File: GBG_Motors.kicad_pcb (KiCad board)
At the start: 2 copper layers, 54 parts, among them J101 Input, J102 Seeed XIAO L, J103 Seeed XIAO R, J104 Pin, J105 Pout, J601 Limit Switch, J701 Limit Switch, Q602 NPN, Q701 NPN, U101 JK Controller, U102 HL Controller, U103 R-78E5.0-0.5, U601 NE555P, U701 NE555P

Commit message: Finished initial board design
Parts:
- JP103: footprint Jumper:SolderJumper-2_P1.3mm_Bridged_RoundedPad1.0x1.5mm -> Jumper:SolderJumper-2_P1.3mm_Open_RoundedPad1.0x1.5mm
- U102: moved to B.Cu
- moved J601 142.7 mm to (122.0, 73.2)
- moved JP603 131.8 mm to (139.5, 94.2)
- moved R607 128.8 mm to (131.9, 110.0), turned to 90 degrees
- moved U101 127.3 mm to (169.9, 101.2), turned to 90 degrees
- moved JP602 118.9 mm to (159.5, 103.9)
- moved U102 117.2 mm to (169.9, 80.4), turned to -90 degrees
- moved C602 115.3 mm to (131.9, 99.8), turned to 90 degrees
- moved U601 114.9 mm to (143.3, 107.4), turned to 180 degrees
- moved JP601 112.5 mm to (158.9, 108.7)
- moved R602 110.2 mm to (154.2, 102.4), turned to -90 degrees
- moved R605 109.7 mm to (147.1, 99.8), turned to 90 degrees
- moved R604 106.5 mm to (150.7, 92.2), turned to -90 degrees
- moved R601 101.1 mm to (161.3, 92.2), turned to -90 degrees
- moved R603 101.1 mm to (157.8, 92.2), turned to -90 degrees
- moved Q601 100.0 mm to (147.6, 104.9), turned to -90 degrees
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- renumbered JP602 to JP601, JP601 to JP602, JP802 to JP801, JP803 to JP802, Q602 to Q601, R607 to R605, R605 to R607
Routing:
- net +5V: track 0.00 -> 173.6 mm, vias 0 -> 6
- net GND: track 0.00 -> 112.2 mm, vias 0 -> 5
- net Hs: track 0.00 -> 71.9 mm
- net /HLBlockerH/input_limited: track 0.00 -> 63.9 mm
- net LRi: track 0.00 -> 60.1 mm, vias 0 -> 3
- net Vout: track 0.00 -> 56.6 mm
- net Kc: track 0.00 -> 56.1 mm, vias 0 -> 1
- net HRo: track 0.00 -> 51.4 mm, vias 0 -> 1
- net VDD: track 0.00 -> 49.7 mm, vias 0 -> 1
- net HRi: track 0.00 -> 48.7 mm, vias 0 -> 1
- net Ls: track 0.00 -> 46.2 mm
- net Jc: track 0.00 -> 46.1 mm, vias 0 -> 1
- net KRi: track 0.00 -> 43.2 mm, vias 0 -> 1
- net Hc: track 0.00 -> 38.2 mm, vias 0 -> 1
- net LRo: track 0.00 -> 35.9 mm, vias 0 -> 3
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- added copper zone on B.Cu, net GND
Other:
- board outline added: 69.6 x 41.7 mm
- board text added: "+5V"
- board text added: "0"
- board text added: "1"
- board text added: "2"
- board text added: "201"
- board text added: "301"
- board text added: "501"
- board text added: "555"
- board text added: "6"
- board text added: "7"
- board text added: "8"
- board text added: "9"
- board text added: "BTS7960"
- board text added: "GND"
- board text added: "H"
- board text added: "H DELAY"
- board text added: "Input"
- board text added: "J"
- board text added: "Join @ Vdd≅5V"
- board text added: "K"
- board text added: "L"
- board text added: "L DELAY"
- board text added: "NC"
- board text added: "NO"
- board text added: "PiCO GBGM V1.0"
- board text added: "Pin"
- board text added: "Pout"
- board text added: "VDD"
- board text added: "Vdd"
- board text added: "Vin"
- board text added: "Vout"
- board text added: "XIAO Expn. Port"
- board text added: "inA"
- board text added: "inB"

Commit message: Replaced VDD/5V passthru with fully-fledged pin header
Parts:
- removed JP103: Regulator Bypass, Jumper:SolderJumper-2_P1.3mm_Open_RoundedPad1.0x1.5mm
- added J106: Bypass, Connector_PinHeader_2.54mm:PinHeader_1x03_P2.54mm_Vertical, F.Cu at (117.9, 80.8)
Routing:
- net Vout: track 56.6 -> 60.3 mm
- net Ls: track 46.2 -> 49.9 mm
- net VDD: track 49.7 -> 51.8 mm
- net Hs: track 71.9 -> 73.5 mm
- net +5V: track 173.6 -> 174.6 mm
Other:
- board text added: "Vdd≅5V"
- board text removed: "Join @ Vdd≅5V"

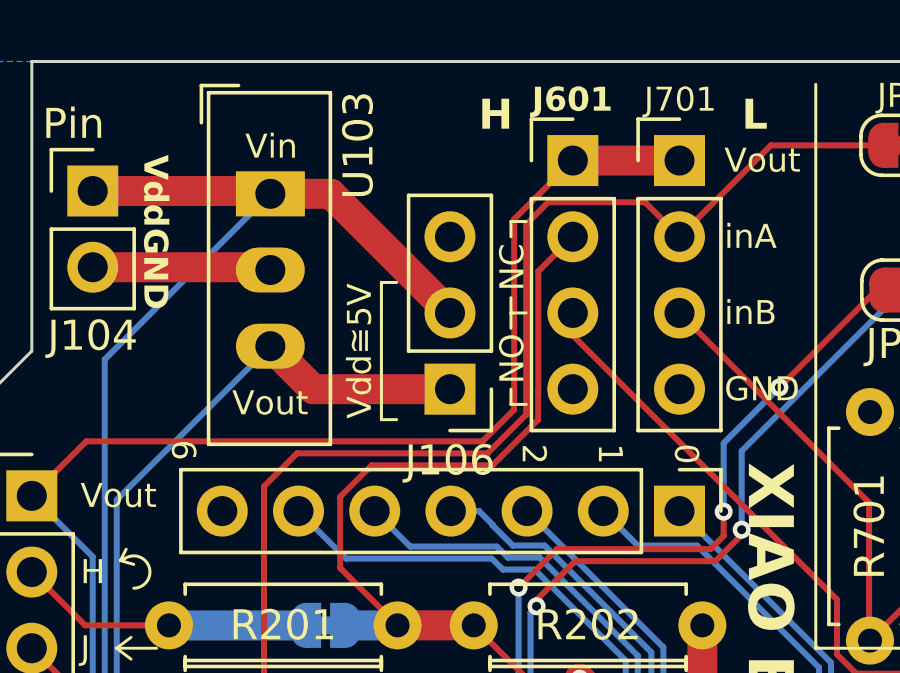
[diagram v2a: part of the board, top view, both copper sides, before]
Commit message: Updated bypass jumper's silkscreen label position
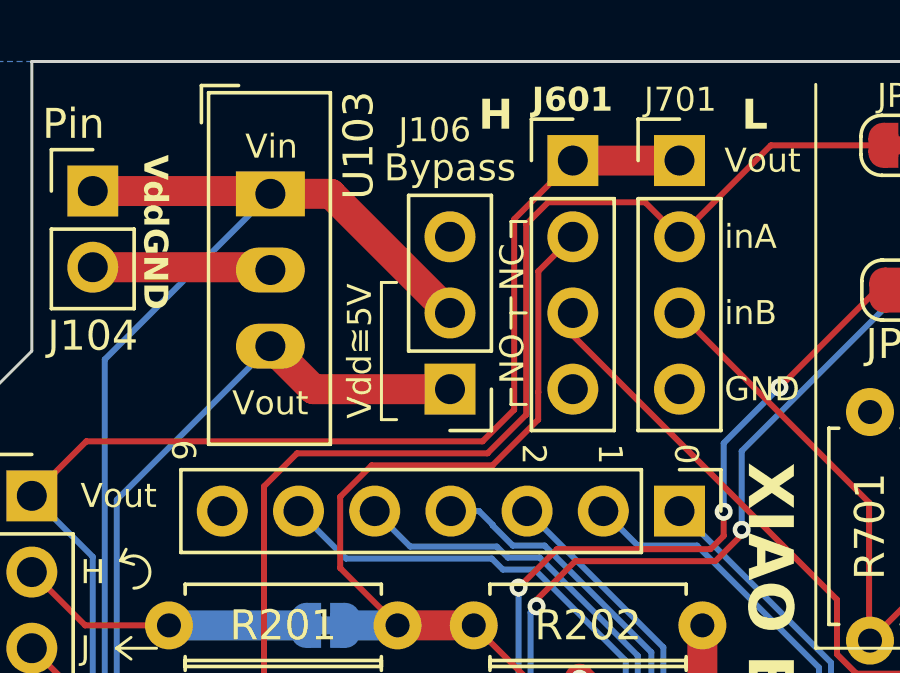
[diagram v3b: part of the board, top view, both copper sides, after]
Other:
- board text added: "Bypass"
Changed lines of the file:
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@@
 			(outputformat 1)
 			(mirror no)
-			(drillshape 1)
+			(drillshape 0)
 			(scaleselection 1)
-			(outputdirectory "")
+			(outputdirectory "Gerbers/")
 		)
 	)
@@
 		(tags "Through hole pin header THT 1x03 2.54mm single row")
 		(property "Reference" "J106"
-			(at 0 -2.38 180)
+			(at 0.508 8.636 180)
 			(layer "F.SilkS")
 			(effects
 				(font
-					(size 1 1)
+					(size 0.8 0.8)
 					(thickness 0.15)
 				)
@@
 			)
 			(justify bottom)
+		)
+	)
+	(gr_text "Bypass"
+		(at 117.856 73.922 0)
+		(layer "F.SilkS")
+		(effects
+			(font
+				(size 0.9 0.9)
+				(thickness 0.1)
+			)
+			(justify bottom)

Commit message: Added bypass capacitor
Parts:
- added C102: 0.22uF, Capacitor_THT:C_Axial_L3.8mm_D2.6mm_P7.50mm_Horizontal, F.Cu at (115.6, 73.2)
- U103: value R-78E5.0-0.5 -> LM7805_TO220; footprint Converter_DCDC:Converter_DCDC_RECOM_R-78E-0.5_THT -> Package_TO_SOT_THT:TO-220-3_Vertical
- moved J106 5.30 mm to (119.4, 75.7), turned to 0 degrees
- moved U103 1.64 mm to (110.2, 74.2)
- moved J601 0.99 mm to (122.9, 73.2)
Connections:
- J106 pad 1: +5V -> VDD
- J106 pad 2: VDD -> +5V
- J106 pad 3: unconnected-(J106-Pin_3-Pad3) -> Net-(J106-Pin_3)
- U103 pad 3: +5V -> Net-(J106-Pin_3)
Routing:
- net GND: track 112.2 -> 122.7 mm
- net Net-(J106-Pin_3): track 0.00 -> 9.99 mm
- net VDD: track 51.8 -> 54.5 mm
- net Hs: track 73.5 -> 74.2 mm
- net +5V: track 174.6 -> 175.4 mm
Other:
- board text added: "[HL]"
- board text added: "[JK]"

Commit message: Final changes based on BoM
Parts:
- removed R602, R702: 10k, Resistor_THT:R_Axial_DIN0207_L6.3mm_D2.5mm_P7.62mm_Horizontal
- R201, R301, R401, R501: value RA -> 1k
- R202, R302, R402, R502: value RB -> 2k
- R601, R701: value R -> 10k
